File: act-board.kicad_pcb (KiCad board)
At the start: 2 copper layers, 15 parts, among them P1 B6B-PH-K-S(LF)(SN), P2 S2B-PH-K-S(LF)(SN), Q1 PN2222A, Q2 IRLB8721PBF, Q3 PN2222A, Q4 PN2222A

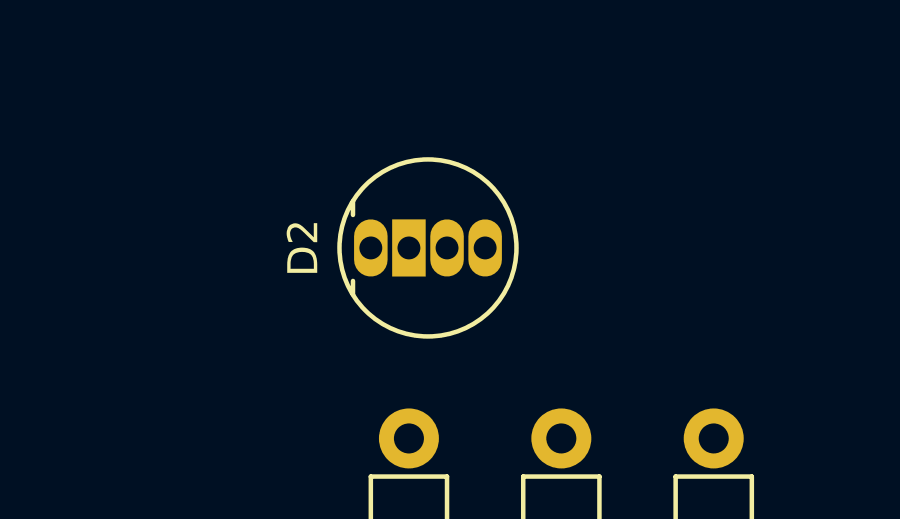
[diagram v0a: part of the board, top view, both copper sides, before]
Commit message: Fix RGB LED pad.
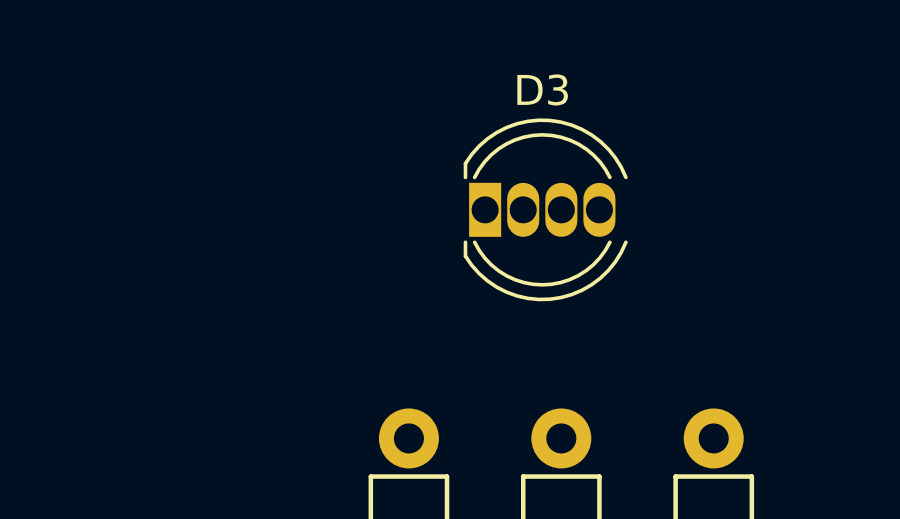
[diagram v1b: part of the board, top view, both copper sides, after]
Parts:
- removed D2: FD-5WSRGB-A, LEDs:LED-RGB-5MM_Common_Cathode
- added D3: FD-5WSRGB-A, LEDs:LED_D5.0mm-4, F.Cu at (144.8, 83.8)
